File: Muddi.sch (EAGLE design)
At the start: 8 parts, among them J1 DCJ0202

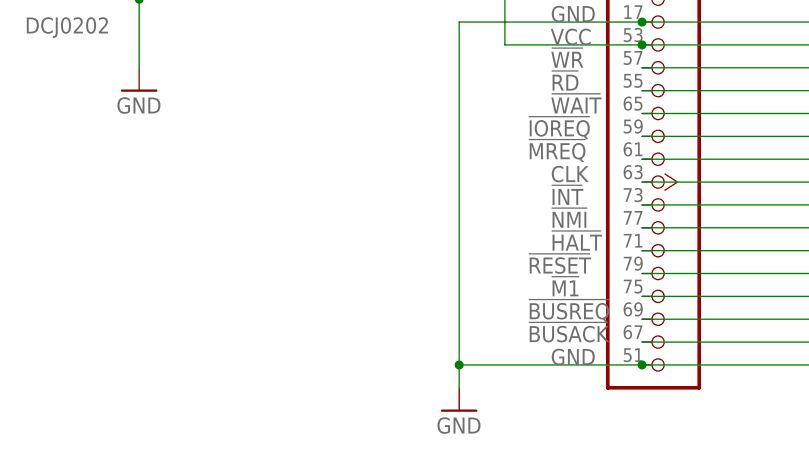
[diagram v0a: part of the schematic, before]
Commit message: Move away Serial CF
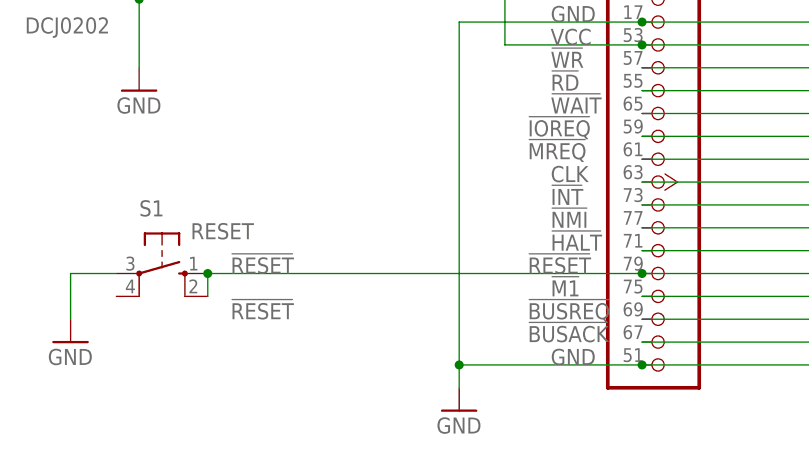
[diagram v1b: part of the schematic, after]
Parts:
- added S1: RESET, switch-omron:10-XX
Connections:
- net GND: now also S1.P
- net N$40: now also S1.S, S1.S1
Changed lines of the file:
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@@
 <part name="P+2" library="supply1" deviceset="VCC" device=""/>
 <part name="GND2" library="supply1" deviceset="GND" device=""/>
+<part name="S1" library="switch-omron" deviceset="10-XX" device="" value="RESET">
+<attribute name="MF" value="OMRON ELECTRONIC COMPONENTS"/>
+</part>
+<part name="GND9" library="supply1" deviceset="GND" device=""/>
 </parts>
 <sheets>
@@
 <instance part="P+2" gate="VCC" x="-17.78" y="213.36"/>
 <instance part="GND2" gate="1" x="-22.86" y="99.06"/>
+<instance part="S1" gate="1" x="-55.88" y="114.3" rot="R270"/>
+<instance part="GND9" gate="1" x="-66.04" y="106.68"/>
 </instances>
 <busses>
@@
 <wire x1="172.72" y1="114.3" x2="134.62" y2="114.3" width="0.1524" layer="91"/>
 <junction x="134.62" y="114.3"/>
+<pinref part="S1" gate="1" pin="S"/>
+<wire x1="-2.54" y1="114.3" x2="-50.8" y2="114.3" width="0.1524" layer="91"/>
+<junction x="-2.54" y="114.3"/>
+<pinref part="S1" gate="1" pin="S1"/>
+<wire x1="-50.8" y1="114.3" x2="-50.8" y2="111.76" width="0.1524" layer="91"/>
+<junction x="-50.8" y="114.3"/>
 </segment>
 </net>
@@
 <junction x="-22.86" y="104.14"/>
 </segment>
-</net>
+<segment>
+<pinref part="GND9" gate="1" pin="GND"/>
+<wire x1="-66.04" y1="109.22" x2="-66.04" y2="114.3" width="0.1524" layer="91"/>
+<pinref part="S1" gate="1" pin="P"/>
+<wire x1="-66.04" y1="114.3" x2="-60.96" y2="114.3" width="0.1524" layer="91"/>
+</segment>
+</net>
+<net name="!RESET" class="0">
+<segment>
+<label x="-48.26" y="114.3" size="1.778" layer="95"/>
+<label x="-48.26" y="109.22" size="1.778" layer="95"/>
+</segment>
+</net>

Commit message: Finish Modularization
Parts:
- added LED1: (no value), led:LED5MM
- added R1: (no value), resistor:R-EU_0207/2V
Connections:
- new net N$25: LED1.A, R1.1
- net GND: now also LED1.C
- net VCC: now also R1.2
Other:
- moved on the sheet: D1, J1
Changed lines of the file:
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@@
 </part>
 <part name="GND9" library="supply1" deviceset="GND" device=""/>
+<part name="LED1" library="led" deviceset="LED" device="5MM"/>
+<part name="R1" library="resistor" deviceset="R-EU_" device="0207/2V"/>
 </parts>
 <sheets>
@@
 <instance part="JP5" gate="A" x="137.16" y="172.72"/>
 <instance part="JP6" gate="A" x="175.26" y="172.72"/>
-<instance part="J1" gate="G$1" x="-68.58" y="147.32"/>
-<instance part="GND" gate="1" x="-58.42" y="134.62"/>
-<instance part="VCC" gate="VCC" x="-58.42" y="160.02"/>
-<instance part="D1" gate="1" x="-45.72" y="147.32" rot="R90">
-<attribute name="OC_FARNELL" x="-45.72" y="147.32" size="1.778" layer="96" display="off"/>
-<attribute name="MF" x="-45.72" y="147.32" size="1.778" layer="96" display="off"/>
-<attribute name="MPN" x="-45.72" y="147.32" size="1.778" layer="96" display="off"/>
+<instance part="J1" gate="G$1" x="2.54" y="254"/>
+<instance part="GND" gate="1" x="12.7" y="241.3"/>
+<instance part="VCC" gate="VCC" x="12.7" y="266.7"/>
+<instance part="D1" gate="1" x="25.4" y="254" rot="R90">
+<attribute name="OC_FARNELL" x="25.4" y="254" size="1.778" layer="96" display="off"/>
+<attribute name="MF" x="25.4" y="254" size="1.778" layer="96" display="off"/>
+<attribute name="MPN" x="25.4" y="254" size="1.778" layer="96" display="off"/>
 </instance>
 <instance part="P+2" gate="VCC" x="-17.78" y="213.36"/>
@@
 <instance part="S1" gate="1" x="-55.88" y="114.3" rot="R270"/>
 <instance part="GND9" gate="1" x="-66.04" y="106.68"/>
+<instance part="LED1" gate="G$1" x="43.18" y="254"/>
+<instance part="R1" gate="G$1" x="43.18" y="264.16" rot="R90"/>
 </instances>
 <busses>
@@
 <segment>
 <pinref part="VCC" gate="VCC" pin="VCC"/>
-<wire x1="-58.42" y1="157.48" x2="-58.42" y2="149.86" width="0.1524" layer="91"/>
+<wire x1="12.7" y1="264.16" x2="12.7" y2="261.62" width="0.1524" layer="91"/>
 <pinref part="J1" gate="G$1" pin="1"/>
-<wire x1="-58.42" y1="149.86" x2="-60.96" y2="149.86" width="0.1524" layer="91"/>
+<wire x1="12.7" y1="261.62" x2="12.7" y2="256.54" width="0.1524" layer="91"/>
+<wire x1="12.7" y1="256.54" x2="10.16" y2="256.54" width="0.1524" layer="91"/>
 <pinref part="D1" gate="1" pin="C"/>
-<wire x1="-45.72" y1="149.86" x2="-58.42" y2="149.86" width="0.1524" layer="91"/>
-<junction x="-58.42" y="149.86"/>
+<wire x1="25.4" y1="256.54" x2="12.7" y2="256.54" width="0.1524" layer="91"/>
+<junction x="12.7" y="256.54"/>
+<pinref part="R1" gate="G$1" pin="2"/>
+<wire x1="43.18" y1="269.24" x2="17.78" y2="269.24" width="0.1524" layer="91"/>
+<wire x1="17.78" y1="269.24" x2="17.78" y2="261.62" width="0.1524" layer="91"/>
+<wire x1="17.78" y1="261.62" x2="12.7" y2="261.62" width="0.1524" layer="91"/>
+<junction x="12.7" y="261.62"/>
 </segment>
 <segment>
@@
 <segment>
 <pinref part="GND" gate="1" pin="GND"/>
-<wire x1="-58.42" y1="137.16" x2="-58.42" y2="144.78" width="0.1524" layer="91"/>
+<wire x1="12.7" y1="243.84" x2="12.7" y2="248.92" width="0.1524" layer="91"/>
 <pinref part="J1" gate="G$1" pin="3"/>
-<wire x1="-58.42" y1="144.78" x2="-60.96" y2="144.78" width="0.1524" layer="91"/>
+<wire x1="12.7" y1="248.92" x2="12.7" y2="251.46" width="0.1524" layer="91"/>
+<wire x1="12.7" y1="251.46" x2="10.16" y2="251.46" width="0.1524" layer="91"/>
 <pinref part="D1" gate="1" pin="A"/>
-<wire x1="-58.42" y1="144.78" x2="-45.72" y2="144.78" width="0.1524" layer="91"/>
-<junction x="-58.42" y="144.78"/>
+<wire x1="12.7" y1="251.46" x2="25.4" y2="251.46" width="0.1524" layer="91"/>
+<junction x="12.7" y="251.46"/>
+<pinref part="LED1" gate="G$1" pin="C"/>
+<wire x1="43.18" y1="248.92" x2="12.7" y2="248.92" width="0.1524" layer="91"/>
+<junction x="12.7" y="248.92"/>
 </segment>
 <segment>
@@
 </segment>
 </net>
+<net name="N$25" class="0">
+<segment>
+<pinref part="R1" gate="G$1" pin="1"/>
+<pinref part="LED1" gate="G$1" pin="A"/>
+<wire x1="43.18" y1="259.08" x2="43.18" y2="256.54" width="0.1524" layer="91"/>
+</segment>
+</net>

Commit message: Update names and font
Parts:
- LED1: value (none) -> BW
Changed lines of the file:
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@@
 </part>
 <part name="GND9" library="supply1" deviceset="GND" device=""/>
-<part name="LED1" library="led" deviceset="LED" device="5MM"/>
+<part name="LED1" library="led" deviceset="LED" device="5MM" value="BW"/>
 <part name="R1" library="resistor" deviceset="R-EU_" device="0207/2V"/>
 </parts>

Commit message: Add Resistor Value
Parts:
- R1: value (none) -> 560
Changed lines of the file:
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@@
 <part name="GND9" library="supply1" deviceset="GND" device=""/>
 <part name="LED1" library="led" deviceset="LED" device="5MM" value="BW"/>
-<part name="R1" library="resistor" deviceset="R-EU_" device="0207/2V"/>
+<part name="R1" library="resistor" deviceset="R-EU_" device="0207/2V" value="560"/>
 </parts>
 <sheets>

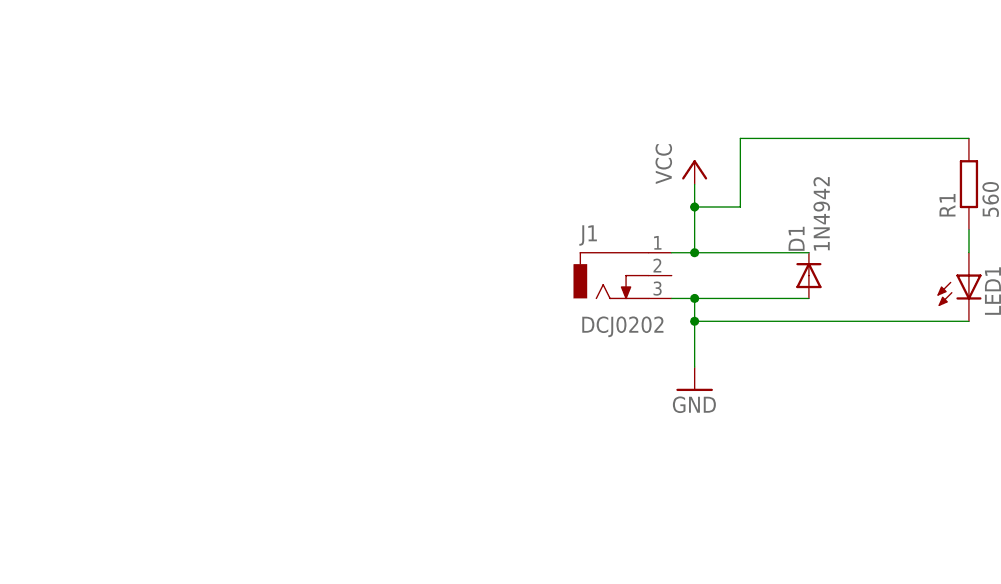
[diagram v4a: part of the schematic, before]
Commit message: Fix MUDDI. Change values to mm.
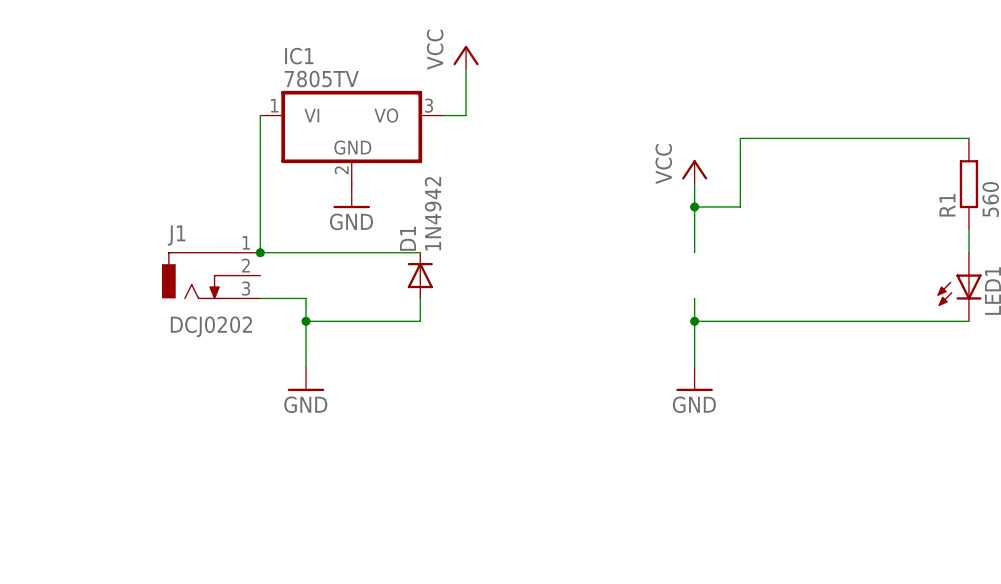
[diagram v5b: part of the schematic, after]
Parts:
- added IC1: 7805TV, linear:7805TV
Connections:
- new net N$26: D1.C, IC1.VI, J1.1
- net GND: now also IC1.GND
- net VCC: now also IC1.VO; no longer D1.C, J1.1
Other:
- moved on the sheet: D1, J1
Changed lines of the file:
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@@
 <part name="LED1" library="led" deviceset="LED" device="5MM" value="BW"/>
 <part name="R1" library="resistor" deviceset="R-EU_" device="0207/2V" value="560"/>
+<part name="IC1" library="linear" deviceset="78*" device="TV" technology="05"/>
+<part name="P+1" library="supply1" deviceset="VCC" device=""/>
+<part name="GND1" library="supply1" deviceset="GND" device=""/>
+<part name="GND3" library="supply1" deviceset="GND" device=""/>
 </parts>
 <sheets>
@@
 <instance part="JP5" gate="A" x="137.16" y="172.72"/>
 <instance part="JP6" gate="A" x="175.26" y="172.72"/>
-<instance part="J1" gate="G$1" x="2.54" y="254"/>
+<instance part="J1" gate="G$1" x="-43.18" y="254"/>
 <instance part="GND" gate="1" x="12.7" y="241.3"/>
 <instance part="VCC" gate="VCC" x="12.7" y="266.7"/>
-<instance part="D1" gate="1" x="25.4" y="254" rot="R90">
-<attribute name="OC_FARNELL" x="25.4" y="254" size="1.778" layer="96" display="off"/>
-<attribute name="MF" x="25.4" y="254" size="1.778" layer="96" display="off"/>
-<attribute name="MPN" x="25.4" y="254" size="1.778" layer="96" display="off"/>
+<instance part="D1" gate="1" x="-17.78" y="254" rot="R90">
+<attribute name="OC_FARNELL" x="-17.78" y="254" size="1.778" layer="96" display="off"/>
+<attribute name="MF" x="-17.78" y="254" size="1.778" layer="96" display="off"/>
+<attribute name="MPN" x="-17.78" y="254" size="1.778" layer="96" display="off"/>
 </instance>
 <instance part="P+2" gate="VCC" x="-17.78" y="213.36"/>
@@
 <instance part="LED1" gate="G$1" x="43.18" y="254"/>
 <instance part="R1" gate="G$1" x="43.18" y="264.16" rot="R90"/>
+<instance part="IC1" gate="A1" x="-25.4" y="271.78"/>
+<instance part="P+1" gate="VCC" x="-12.7" y="279.4"/>
+<instance part="GND1" gate="1" x="-25.4" y="261.62"/>
+<instance part="GND3" gate="1" x="-30.48" y="241.3"/>
 </instances>
 <busses>
@@
 <pinref part="VCC" gate="VCC" pin="VCC"/>
 <wire x1="12.7" y1="264.16" x2="12.7" y2="261.62" width="0.1524" layer="91"/>
-<pinref part="J1" gate="G$1" pin="1"/>
 <wire x1="12.7" y1="261.62" x2="12.7" y2="256.54" width="0.1524" layer="91"/>
-<wire x1="12.7" y1="256.54" x2="10.16" y2="256.54" width="0.1524" layer="91"/>
-<pinref part="D1" gate="1" pin="C"/>
-<wire x1="25.4" y1="256.54" x2="12.7" y2="256.54" width="0.1524" layer="91"/>
-<junction x="12.7" y="256.54"/>
 <pinref part="R1" gate="G$1" pin="2"/>
 <wire x1="43.18" y1="269.24" x2="17.78" y2="269.24" width="0.1524" layer="91"/>
@@
 <junction x="134.62" y="139.7"/>
 </segment>
+<segment>
+<pinref part="IC1" gate="A1" pin="VO"/>
+<pinref part="P+1" gate="VCC" pin="VCC"/>
+<wire x1="-15.24" y1="271.78" x2="-12.7" y2="271.78" width="0.1524" layer="91"/>
+<wire x1="-12.7" y1="271.78" x2="-12.7" y2="276.86" width="0.1524" layer="91"/>
+</segment>
 </net>
 <net name="GND" class="0">
@@
 <pinref part="GND" gate="1" pin="GND"/>
 <wire x1="12.7" y1="243.84" x2="12.7" y2="248.92" width="0.1524" layer="91"/>
-<pinref part="J1" gate="G$1" pin="3"/>
 <wire x1="12.7" y1="248.92" x2="12.7" y2="251.46" width="0.1524" layer="91"/>
-<wire x1="12.7" y1="251.46" x2="10.16" y2="251.46" width="0.1524" layer="91"/>
-<pinref part="D1" gate="1" pin="A"/>
-<wire x1="12.7" y1="251.46" x2="25.4" y2="251.46" width="0.1524" layer="91"/>
-<junction x="12.7" y="251.46"/>
 <pinref part="LED1" gate="G$1" pin="C"/>
 <wire x1="43.18" y1="248.92" x2="12.7" y2="248.92" width="0.1524" layer="91"/>
@@
 <wire x1="-66.04" y1="114.3" x2="-60.96" y2="114.3" width="0.1524" layer="91"/>
 </segment>
+<segment>
+<pinref part="IC1" gate="A1" pin="GND"/>
+<pinref part="GND1" gate="1" pin="GND"/>
+</segment>
+<segment>
+<pinref part="J1" gate="G$1" pin="3"/>
+<pinref part="GND3" gate="1" pin="GND"/>
+<wire x1="-35.56" y1="251.46" x2="-30.48" y2="251.46" width="0.1524" layer="91"/>
+<wire x1="-30.48" y1="251.46" x2="-30.48" y2="248.92" width="0.1524" layer="91"/>
+<pinref part="D1" gate="1" pin="A"/>
+<wire x1="-30.48" y1="248.92" x2="-30.48" y2="243.84" width="0.1524" layer="91"/>
+<wire x1="-17.78" y1="251.46" x2="-17.78" y2="248.92" width="0.1524" layer="91"/>
+<wire x1="-30.48" y1="248.92" x2="-17.78" y2="248.92" width="0.1524" layer="91"/>
+<junction x="-30.48" y="248.92"/>
+</segment>
 </net>
 <net name="!RESET" class="0">
@@
 </segment>
 </net>
+<net name="N$26" class="0">
+<segment>
+<pinref part="J1" gate="G$1" pin="1"/>
+<pinref part="IC1" gate="A1" pin="VI"/>
+<wire x1="-35.56" y1="256.54" x2="-35.56" y2="271.78" width="0.1524" layer="91"/>
+<pinref part="D1" gate="1" pin="C"/>
+<wire x1="-17.78" y1="256.54" x2="-35.56" y2="256.54" width="0.1524" layer="91"/>
+<junction x="-35.56" y="256.54"/>
+</segment>
+</net>

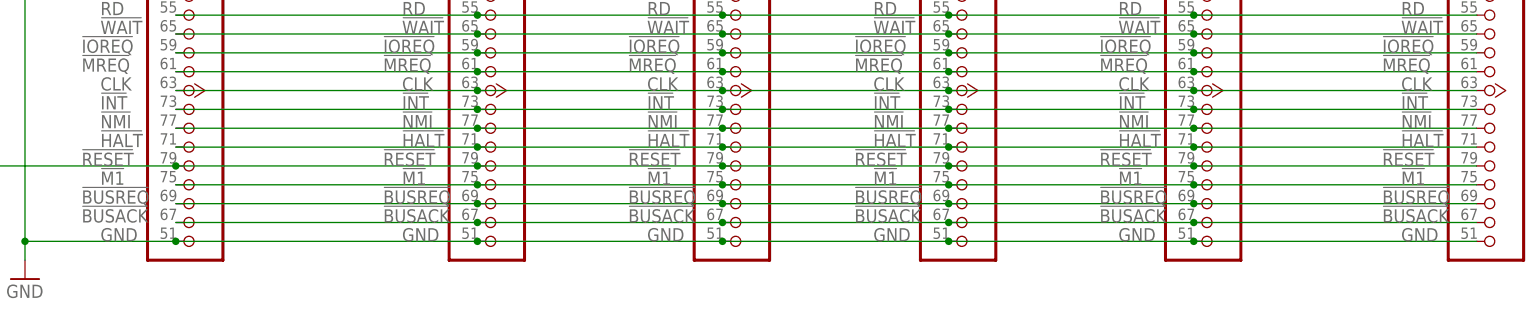
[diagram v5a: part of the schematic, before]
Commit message: Add Ground Rail to JEANNECTOR
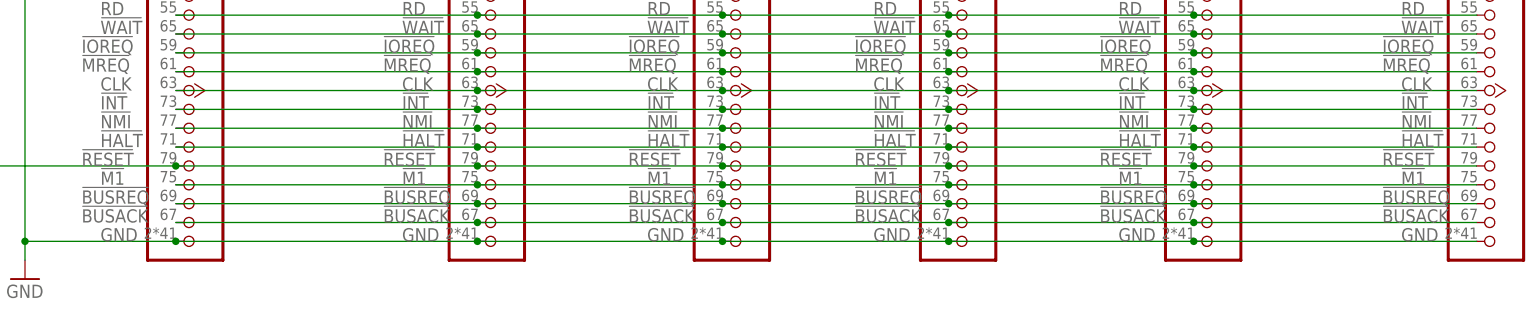
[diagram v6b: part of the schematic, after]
